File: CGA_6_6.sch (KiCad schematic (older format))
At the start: 8 parts, among them P5 Bus_ISA_8bit, U13 74LS08, U14 74LS32, U20 74LS04, U26 74S04, U41 74LS08, U42 74LS86, U66 74LS245

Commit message: More sheet 6
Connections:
- net GND: now also P5.1 (GND), P5.10 (GND), P5.31 (GND), U42.13
- net VCC: now also P5.29 (VCC), P5.3 (VCC)
- net ~SMEMR: now reaches P5.12 (~SMEMR)
- net ~SMEMR: now also U42.12
- net ~IOW: now reaches P5.13 (~IOW)
- net ~IOR: now reaches P5.14 (~IOR)
- net ~IOR: now also U14.10
- net RESET: now reaches P5.2 (RESET)
- net RESET: now also U20.9
- net IOCLK: now reaches P5.20 (CLK)
- net OSC: now reaches P5.30 (OSC)
- net OSC: now also U26.13
- net DB7: now reaches P5.33 (DB7)
- net DB7: now also U66.9 (A7)
- net DB6: now reaches P5.34 (DB6)
- net DB6: now also U66.8 (A6)
- net DB5: now reaches P5.35 (DB5)
- net DB5: now also U66.7 (A5)
- net DB4: now reaches P5.36 (DB4)
- net DB4: now also U66.6 (A4)
- net DB3: now reaches P5.37 (DB3)
- net DB3: now also U66.5 (A3)
- net DB2: now reaches P5.38 (DB2)
- net DB2: now also U66.4 (A2)
- net DB1: now reaches P5.39 (DB1)
- net DB1: now also U66.3 (A1)
- net DB0: now reaches P5.40 (DB0)
- net DB0: now also U66.2 (A0)
- net IO_READY: now reaches P5.41 (IO_READY)
- net AEN: now reaches P5.42 (AEN)
- net AEN: now also U14.9
- net A19: now reaches P5.43 (BA19)
- net A18: now reaches P5.44 (BA18)
- net A17: now reaches P5.45 (BA17)
- net A16: now reaches P5.46 (BA16)
- net A15: now reaches P5.47 (BA15)
- net A14: now reaches P5.48 (BA14)
- net A13: now reaches P5.49 (BA13)
- net A12: now reaches P5.50 (BA12)
- net A11: now reaches P5.51 (BA11)
- net A10: now reaches P5.52 (BA10)
- net A9: now reaches P5.53 (BA09)
- net A8: now reaches P5.54 (BA08)
- net A7: now reaches P5.55 (BA07)
- net A6: now reaches P5.56 (BA06)
- net A5: now reaches P5.57 (BA05)
- net A4: now reaches P5.58 (BA04)
- net A3: now reaches P5.59 (BA03)
- net A2: now reaches P5.60 (BA02)
- net A1: now reaches P5.61 (BA01)
- net at P5.62 (BA00): now also U13.4, U13.5
- net +12V: now reaches P5.9 (+12V)
- net at U66.1 (A->B): now also U41.6
- net D7: now reaches U66.11 (B7)
- net D6: now reaches U66.12 (B6)
- net D5: now reaches U66.13 (B5)
- net D4: now reaches U66.14 (B4)
- net D3: now reaches U66.15 (B3)
- net D2: now reaches U66.16 (B2)
- net D1: now reaches U66.17 (B1)
- net D0: now reaches U66.18 (B0)
- net DATA_GATE: now reaches U66.19 (CE)
- net at U41.4: now also U14.8
- net ~MEMR: now reaches U41.5
- net ~MEMR: now also U42.11
- net A0: now reaches U13.6
- net ~RESET': now reaches U20.8
- net 14_Mhz: now reaches U26.12
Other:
- moved on the sheet: P5, U13B, U14C, U20D, U26F, U41B, U66

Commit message: Sheet 6
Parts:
- added C1, C10, C11, C12, C13, C14, C15, C17, C18, C2, C25, C26, C27, C28, C3, C30, C33, C5, C7, C9: 4.7nF, Capacitor_THT:C_Disc_D4.3mm_W1.9mm_P5.00mm, symbol Device:C_Small
- added C16, C19, C24, C29, C4, C6, C8: 10uF, Capacitor_THT:CP_Radial_D8.0mm_P5.00mm, symbol Device:CP_Small
- added J1: VIDEO JACK, symbol Connector:Conn_Coaxial
- added J2: RGBI Output, symbol Connector:DB9_Female_MountingHoles
- added P1: 1X4 BERG, symbol Connector_Generic:Conn_01x04
- added P2: 1X6 BERG, symbol Connector_Generic:Conn_01x06
- added R11, R12, R13, R14: 30, Resistor_THT:R_Axial_DIN0207_L6.3mm_D2.5mm_P10.16mm_Horizontal, symbol Device:R_Small
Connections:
- net +12V: now also C8.1, C9.2, P1.1 (Pin_1), P2.6 (Pin_6)
- net GND: now also C1.1, C10.1, C11.1, C12.1, C13.1, C14.1, C15.1, C16.2, C17.1, C18.1, C19.2, C2.1, C24.2, C25.1, C26.1, C27.1, C28.1, C29.2, C3.1, C30.1, C33.1, C4.2, C5.1, C6.2, C7.1, C8.2, C9.1, J1.2 (Ext), J2.0 (PAD), J2.1, J2.2, P1.4 (Pin_4), P2.4 (Pin_4)
- net VCC: now also C1.2, C10.2, C11.2, C12.2, C13.2, C14.2, C15.2, C16.1, C17.2, C18.2, C19.1, C2.2, C24.1, C25.2, C26.2, C27.2, C28.2, C29.1, C3.2, C30.2, C33.2, C4.1, C5.2, C6.1, C7.2, P2.5 (Pin_5)
- new net: J2.6, R14.1
- new net: J2.3, R11.1
- new net: J2.4, R12.1
- new net: J2.5, R13.1
- new net B_OUT: R13.2
- new net COMP_VID: J1.1 (In), P1.3 (Pin_3)
- new net G_OUT: R12.2
- new net HSYNC_OUT: J2.8
- new net I_OUT: R14.2
- new net R_OUT: R11.2
- new net VSYNC_OUT: J2.9
- new net ~LPEN_INPUT: P2.1 (Pin_1)
- new net ~LPEN_SW: P2.3 (Pin_3)
- no-connect marks 0 -> 3

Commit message: Fix some more flags and footprints
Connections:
- net ~MEMW: now reaches P5.11 (~SMEMW)
- net 14_Mhz renamed 14_MHZ
- net A14: no longer names the net of P5.48 (BA14)
- net IOCLK renamed IO_CLOCK
- no-connect marks 3 -> 23
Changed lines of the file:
@@
 Text GLabel 9550 2550 2    50   Output ~ 0
 A15
-Text GLabel 9550 2650 2    50   Output ~ 0
-A14
 Text GLabel 9550 2450 2    50   Output ~ 0
 A16
@@
 	2250 5700 2600 5700
 Text GLabel 2600 5700 2    50   Output ~ 0
-14_Mhz
+14_MHZ
 $Comp
 L power:+12V #PWR0218
@@
 	7600 2950 7150 2950
 Text GLabel 7150 2950 0    50   Output ~ 0
-IOCLK
+IO_CLOCK
 Wire Wire Line
 	9000 2050 9550 2050
@@
 ~IOR
 Wire Wire Line
-	7600 1950 6950 1950
-Wire Wire Line
-	6950 1950 6950 2000
+	6700 1950 6700 2000
 $Comp
 L power:GND #PWR0221
 U 1 1 64DF990F
-P 6950 2000
-F 0 "#PWR0221" H 6950 1750 50  0001 C CNN
-F 1 "GND" H 6955 1827 50  0000 C CNN
-F 2 "" H 6950 2000 50  0001 C CNN
-F 3 "" H 6950 2000 50  0001 C CNN
-	1    6950 2000
+P 6700 2000
+F 0 "#PWR0221" H 6700 1750 50  0001 C CNN
+F 1 "GND" H 6705 1827 50  0000 C CNN
+F 2 "" H 6700 2000 50  0001 C CNN
+F 3 "" H 6700 2000 50  0001 C CNN
+	1    6700 2000
 	1    0    0    -1
 $EndComp
@@
 $EndComp
 Connection ~ 6050 4350
+NoConn ~ 7600 1350
+NoConn ~ 7600 1450
+NoConn ~ 7600 1550
+NoConn ~ 7600 1650
+NoConn ~ 7600 1750
+NoConn ~ 7600 2450
+NoConn ~ 7600 2550
+NoConn ~ 7600 2650
+NoConn ~ 7600 2750
+NoConn ~ 7600 2850
+NoConn ~ 7600 3050
+NoConn ~ 7600 3150
+NoConn ~ 7600 3250
+NoConn ~ 7600 3350
+NoConn ~ 7600 3450
+NoConn ~ 7600 3550
+NoConn ~ 7600 3650
+NoConn ~ 7600 3750
+NoConn ~ 9000 1050
+Wire Wire Line
+	6700 1950 7600 1950
+Wire Wire Line
+	7600 2050 7050 2050
+Text GLabel 7050 2050 0    50   Output ~ 0
+~MEMW
+NoConn ~ 9550 2650
 $EndSCHEMATC

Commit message: Add note on light pen input and change the label types
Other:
- note added: "Light pen\nconnector"
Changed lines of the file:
@@
 U 1 1 64ED37DC
 P 5850 3450
-F 0 "P2" H 6000 3350 50  0000 C CNN
-F 1 "1X6 BERG" H 6100 3450 50  0000 C CNN
+F 0 "P2" H 6000 3500 50  0000 C CNN
+F 1 "1X6 BERG" H 6100 3600 50  0000 C CNN
 F 2 "" H 5850 3450 50  0001 C CNN
 F 3 "~" H 5850 3450 50  0001 C CNN
@@
 Wire Wire Line
 	4600 3350 4600 3400
-Text GLabel 5250 3450 0    50   Input ~ 0
+Text GLabel 5250 3450 0    50   Output ~ 0
 ~LPEN_SW
-Text GLabel 5250 3650 0    50   Input ~ 0
+Text GLabel 5250 3650 0    50   Output ~ 0
 ~LPEN_INPUT
 Wire Wire Line
@@
 ~MEMW
 NoConn ~ 9550 2650
+Text Notes 5950 3300 0    50   ~ 0
+Light pen\nconnector
 $EndSCHEMATC

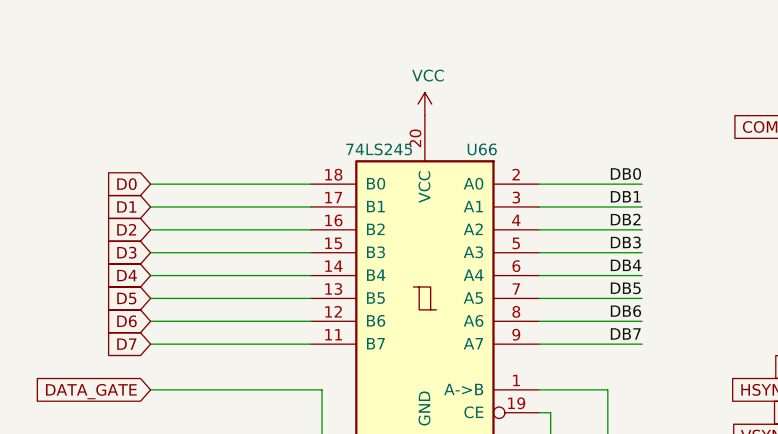
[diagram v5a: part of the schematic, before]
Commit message: Add extra libraries and assign footprints
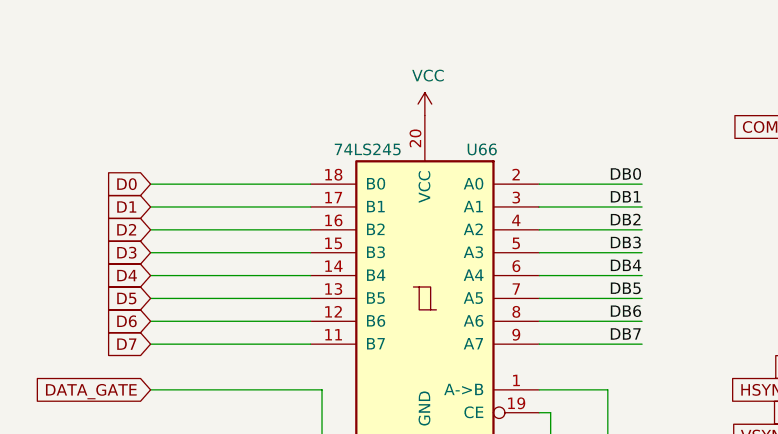
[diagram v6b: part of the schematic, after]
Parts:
- J1: footprint (none) -> w_conn_av:rca_yellow
- J2: footprint (none) -> Connector_Dsub:DSUB-9_Female_Horizontal_P2.77x2.84mm_EdgePinOffset7.70mm_Housed_MountingHolesOffset9.12mm
- P1: footprint (none) -> Connector_PinHeader_2.54mm:PinHeader_1x04_P2.54mm_Vertical
- P2: footprint (none) -> Connector_PinHeader_2.54mm:PinHeader_1x05_P2.54mm_Vertical
- P5: footprint (none) -> My_Components:Conn_Edge_PCB_ISA8
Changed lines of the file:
@@
 F 0 "P5" H 8300 4317 50  0000 C CNN
 F 1 "Bus_ISA_8bit" H 8300 4226 50  0000 C CNN
-F 2 "" H 8300 2550 50  0001 C CNN
+F 2 "My_Components:Conn_Edge_PCB_ISA8" H 8300 2550 50  0001 C CNN
 F 3 "https://en.wikipedia.org/wiki/Industry_Standard_Architecture" H 8300 2550 50  0001 C CNN
 	1    8300 2550
@@
 P 2600 1800
 F 0 "U66" H 2350 2450 50  0000 C CNN
-F 1 "74LS245" H 2800 2450 50  0000 C CNN
+F 1 "74LS245" H 2850 2450 50  0000 C CNN
 F 2 "Package_DIP:DIP-20_W7.62mm_LongPads" H 2600 1800 50  0001 C CNN
 F 3 "http://www.ti.com/lit/gpn/sn74LS245" H 2600 1800 50  0001 C CNN
@@
 F 0 "J1" H 5050 1025 50  0000 L CNN
 F 1 "VIDEO JACK" H 5050 934 50  0000 L CNN
-F 2 "" H 4950 1050 50  0001 C CNN
+F 2 "w_conn_av:rca_yellow" H 4950 1050 50  0001 C CNN
 F 3 " ~" H 4950 1050 50  0001 C CNN
 	1    4950 1050
@@
 F 0 "P1" H 6018 625 50  0000 C CNN
 F 1 "1X4 BERG" H 6018 716 50  0000 C CNN
-F 2 "" H 6100 1050 50  0001 C CNN
+F 2 "Connector_PinHeader_2.54mm:PinHeader_1x04_P2.54mm_Vertical" H 6100 1050 50  0001 C CNN
 F 3 "~" H 6100 1050 50  0001 C CNN
 	1    6100 1050
@@
 F 0 "J2" H 6080 2102 50  0000 L CNN
 F 1 "RGBI Output" H 6080 2011 50  0000 L CNN
-F 2 "" H 5900 2100 50  0001 C CNN
+F 2 "Connector_Dsub:DSUB-9_Female_Horizontal_P2.77x2.84mm_EdgePinOffset7.70mm_Housed_MountingHolesOffset9.12mm" H 5900 2100 50  0001 C CNN
 F 3 " ~" H 5900 2100 50  0001 C CNN
 	1    5900 2100
@@
 F 0 "P2" H 6000 3500 50  0000 C CNN
 F 1 "1X6 BERG" H 6100 3600 50  0000 C CNN
-F 2 "" H 5850 3450 50  0001 C CNN
+F 2 "Connector_PinHeader_2.54mm:PinHeader_1x05_P2.54mm_Vertical" H 5850 3450 50  0001 C CNN
 F 3 "~" H 5850 3450 50  0001 C CNN
 	1    5850 3450

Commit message: Fixed some footprints
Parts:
- C16, C19, C24, C29, C4, C6, C8: footprint Capacitor_THT:CP_Radial_D8.0mm_P5.00mm -> Capacitor_THT:CP_Radial_D5.0mm_P2.50mm
- P2: footprint Connector_PinHeader_2.54mm:PinHeader_1x05_P2.54mm_Vertical -> Connector_PinHeader_2.54mm:PinHeader_1x06_P2.54mm_Vertical
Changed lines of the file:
@@
 F 0 "P2" H 6000 3500 50  0000 C CNN
 F 1 "1X6 BERG" H 6100 3600 50  0000 C CNN
-F 2 "Connector_PinHeader_2.54mm:PinHeader_1x05_P2.54mm_Vertical" H 5850 3450 50  0001 C CNN
+F 2 "Connector_PinHeader_2.54mm:PinHeader_1x06_P2.54mm_Vertical" H 5850 3450 50  0001 C CNN
 F 3 "~" H 5850 3450 50  0001 C CNN
 	1    5850 3450
@@
 F 0 "C24" V 5150 4300 50  0000 C CNN
 F 1 "10uF" V 5150 4050 50  0000 C CNN
-F 2 "Capacitor_THT:CP_Radial_D8.0mm_P5.00mm" H 5100 4200 50  0001 C CNN
+F 2 "Capacitor_THT:CP_Radial_D5.0mm_P2.50mm" H 5100 4200 50  0001 C CNN
 F 3 "~" H 5100 4200 50  0001 C CNN
 	1    5100 4200
@@
 F 0 "C29" V 5150 4450 50  0000 C CNN
 F 1 "10uF" V 5150 4200 50  0000 C CNN
-F 2 "Capacitor_THT:CP_Radial_D8.0mm_P5.00mm" H 5100 4350 50  0001 C CNN
+F 2 "Capacitor_THT:CP_Radial_D5.0mm_P2.50mm" H 5100 4350 50  0001 C CNN
 F 3 "~" H 5100 4350 50  0001 C CNN
 	1    5100 4350
@@
 F 0 "C4" V 5150 4600 50  0000 C CNN
 F 1 "10uF" V 5150 4350 50  0000 C CNN
-F 2 "Capacitor_THT:CP_Radial_D8.0mm_P5.00mm" H 5100 4500 50  0001 C CNN
+F 2 "Capacitor_THT:CP_Radial_D5.0mm_P2.50mm" H 5100 4500 50  0001 C CNN
 F 3 "~" H 5100 4500 50  0001 C CNN
 	1    5100 4500
@@
 F 0 "C19" V 5150 4750 50  0000 C CNN
 F 1 "10uF" V 5150 4500 50  0000 C CNN
-F 2 "Capacitor_THT:CP_Radial_D8.0mm_P5.00mm" H 5100 4650 50  0001 C CNN
+F 2 "Capacitor_THT:CP_Radial_D5.0mm_P2.50mm" H 5100 4650 50  0001 C CNN
 F 3 "~" H 5100 4650 50  0001 C CNN
 	1    5100 4650
@@
 F 0 "C16" V 5150 4900 50  0000 C CNN
 F 1 "10uF" V 5150 4650 50  0000 C CNN
-F 2 "Capacitor_THT:CP_Radial_D8.0mm_P5.00mm" H 5100 4800 50  0001 C CNN
+F 2 "Capacitor_THT:CP_Radial_D5.0mm_P2.50mm" H 5100 4800 50  0001 C CNN
 F 3 "~" H 5100 4800 50  0001 C CNN
 	1    5100 4800
@@
 F 0 "C6" V 5150 5050 50  0000 C CNN
 F 1 "10uF" V 5150 4800 50  0000 C CNN
-F 2 "Capacitor_THT:CP_Radial_D8.0mm_P5.00mm" H 5100 4950 50  0001 C CNN
+F 2 "Capacitor_THT:CP_Radial_D5.0mm_P2.50mm" H 5100 4950 50  0001 C CNN
 F 3 "~" H 5100 4950 50  0001 C CNN
 	1    5100 4950
@@
 F 0 "C8" V 5800 4300 50  0000 C CNN
 F 1 "10uF" V 5800 4050 50  0000 C CNN
-F 2 "Capacitor_THT:CP_Radial_D8.0mm_P5.00mm" H 5750 4200 50  0001 C CNN
+F 2 "Capacitor_THT:CP_Radial_D5.0mm_P2.50mm" H 5750 4200 50  0001 C CNN
 F 3 "~" H 5750 4200 50  0001 C CNN
 	1    5750 4200

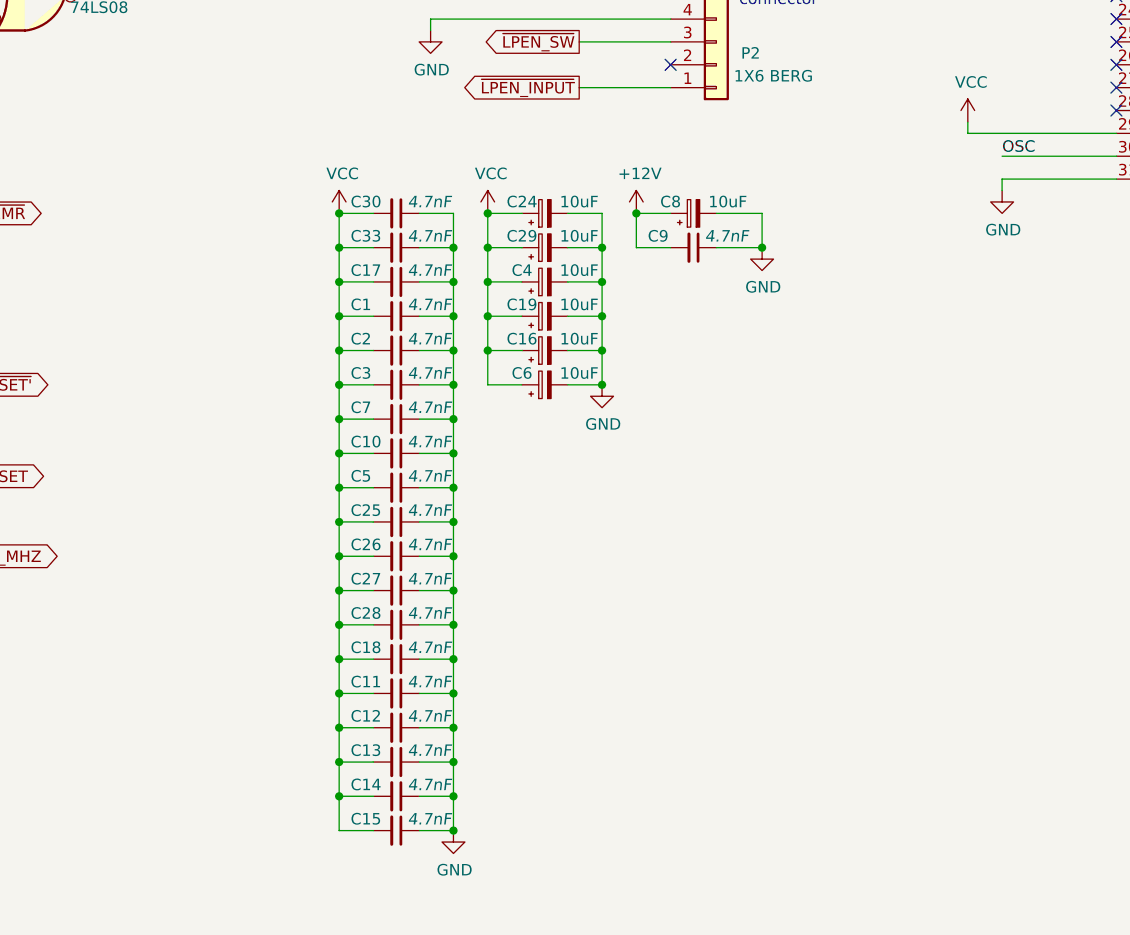
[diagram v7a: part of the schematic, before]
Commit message: Add filter caps for every IC
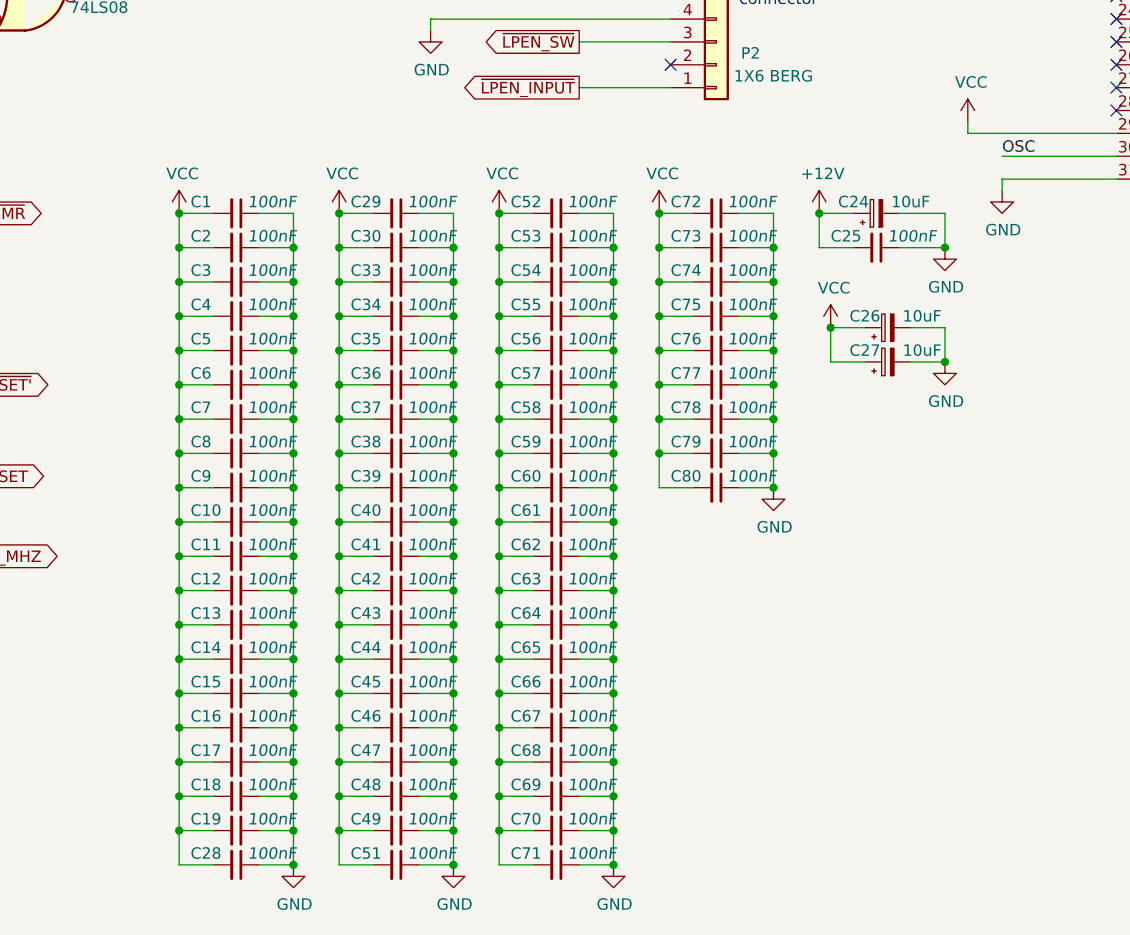
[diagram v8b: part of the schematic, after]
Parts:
- removed C1, C25, C26, C27: 4.7nF, Capacitor_THT:C_Disc_D4.3mm_W1.9mm_P5.00mm, symbol Device:C_Small
- removed C16, C19, C4, C6: 10uF, Capacitor_THT:CP_Radial_D5.0mm_P2.50mm, symbol Device:CP_Small
- added C16, C19, C29, C30, C34, C35, C36, C37, C38, C39, C4, C40, C41, C42, C43, C44, C45, C46, C47, C48, C49, C51, C52, C53, C54, C55, C56, C57, C58, C59, C6, C60, C61, C62, C63, C64, C65, C66, C67, C68, C69, C70, C71, C72, C73, C74, C75, C76, C77, C78, C79, C8, C80, C9: 100nF, Capacitor_THT:C_Disc_D4.3mm_W1.9mm_P5.00mm, symbol Device:C_Small
- C1: renamed from C30; value 4.7nF -> 100nF
- C10, C11, C12, C13, C14, C15, C17, C18, C2, C28, C3, C33, C5, C7: value 4.7nF -> 100nF
- C25: renamed from C9; value 4.7nF -> 100nF
- renumbered C8 to C24, C24 to C26, C29 to C27
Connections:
- net GND: now also C16.1, C19.1, C29.1, C30.1, C34.1, C35.1, C36.1, C37.1, C38.1, C39.1, C4.1, C40.1, C41.1, C42.1, C43.1, C44.1, C45.1, C46.1, C47.1, C48.1, C49.1, C51.1, C52.1, C53.1, C54.1, C55.1, C56.1, C57.1, C58.1, C59.1, C6.1, C60.1, C61.1, C62.1, C63.1, C64.1, C65.1, C66.1, C67.1, C68.1, C69.1, C70.1, C71.1, C72.1, C73.1, C74.1, C75.1, C76.1, C77.1, C78.1, C79.1, C8.1, C80.1, C9.1
- net VCC: now also C16.2, C19.2, C29.2, C30.2, C34.2, C35.2, C36.2, C37.2, C38.2, C39.2, C4.2, C40.2, C41.2, C42.2, C43.2, C44.2, C45.2, C46.2, C47.2, C48.2, C49.2, C51.2, C52.2, C53.2, C54.2, C55.2, C56.2, C57.2, C58.2, C59.2, C6.2, C60.2, C61.2, C62.2, C63.2, C64.2, C65.2, C66.2, C67.2, C68.2, C69.2, C70.2, C71.2, C72.2, C73.2, C74.2, C75.2, C76.2, C77.2, C78.2, C79.2, C8.2, C80.2, C9.2
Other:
- moved on the sheet: C1, C24, C25, C26, C27
